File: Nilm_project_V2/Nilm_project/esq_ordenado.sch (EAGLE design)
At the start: 37 parts, among them IC1 LM1117IMPX-3.3, Q1 SMD-TRANSISTORS-NPN-25V-500MW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, Q2 SMD-TRANSISTORS-NPN-25V-500MW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, U1 ESP-32S, U2 CP2102-GM, U3 TPD2S017DBVR, U4 SP0503BAHT

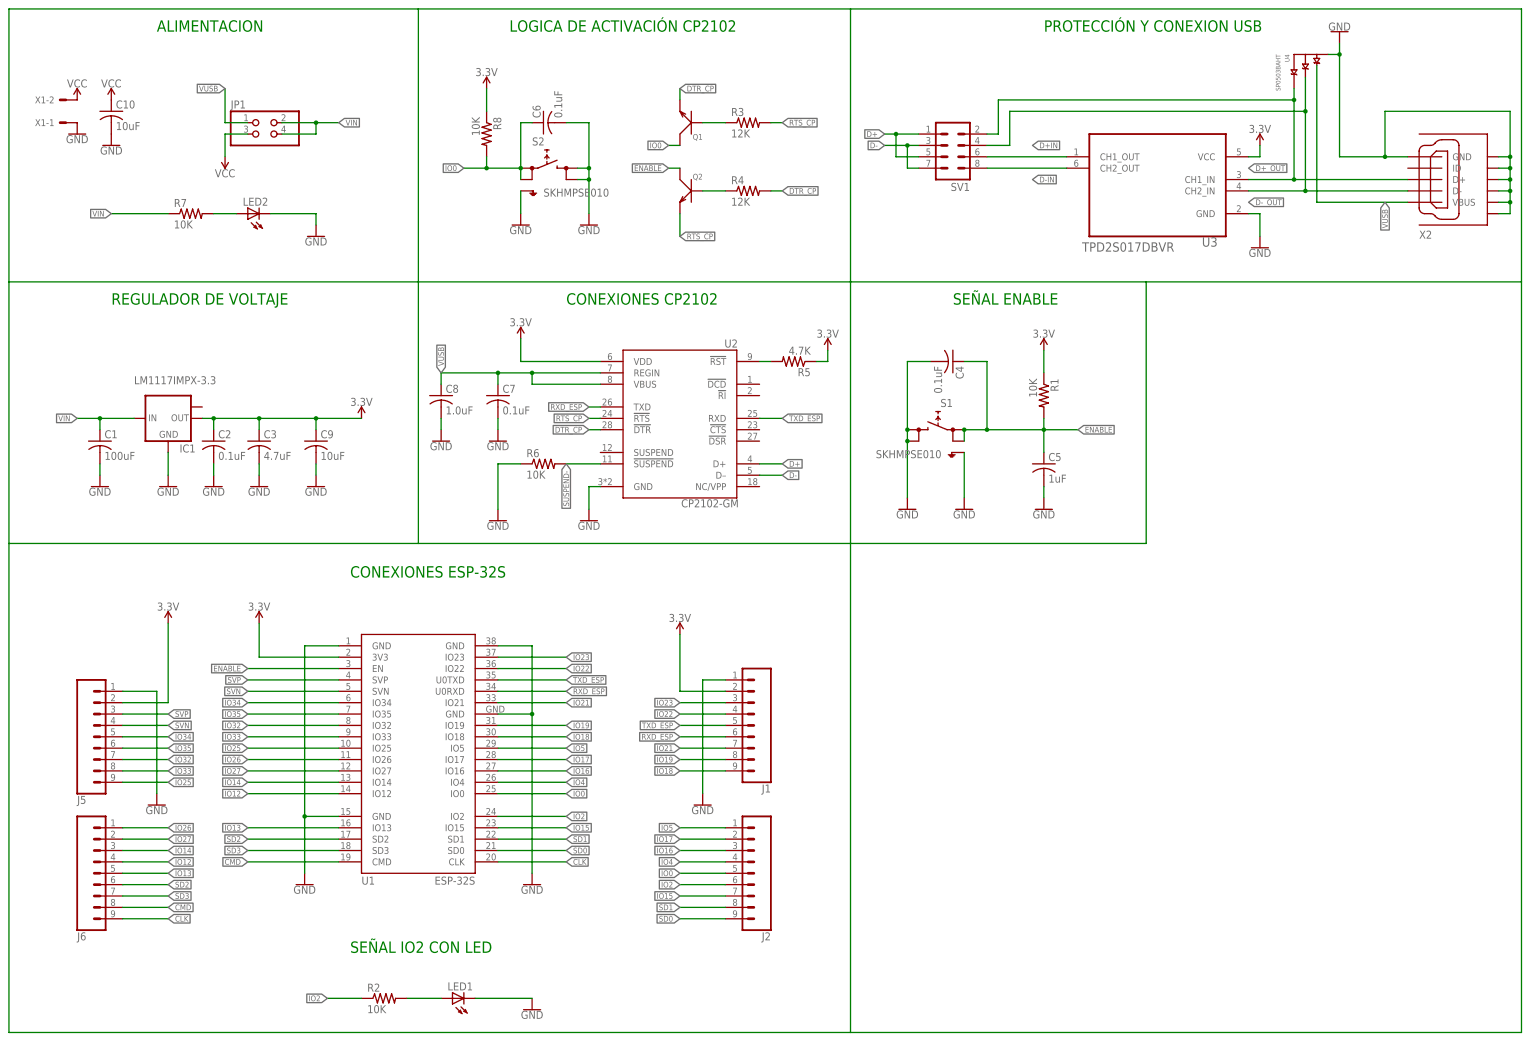
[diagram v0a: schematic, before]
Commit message: actualizacion de datahseets, lista de elementos, esquematico terminado
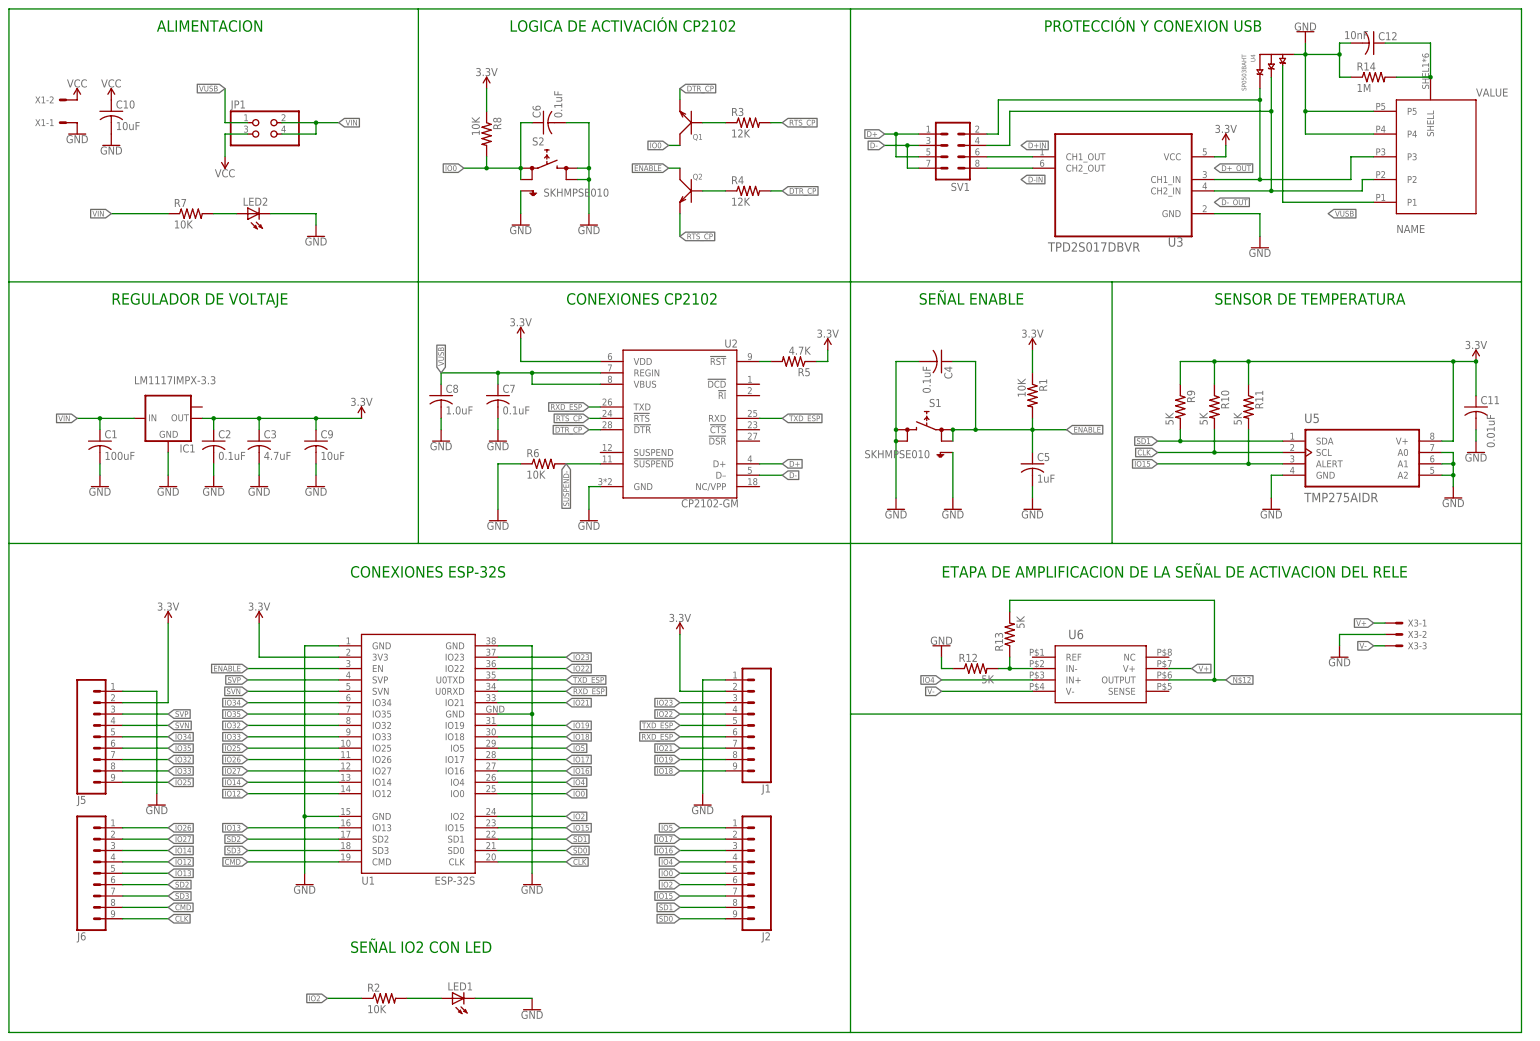
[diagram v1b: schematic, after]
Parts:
- removed X2: (no value), BeagleBone_Blue_R3:10118192-0001LF
- added C11: 0.01uF, resistor:C-USC0805
- added C12: 10nF, resistor:C-USC0805
- added R10, R11, R12, R13, R9: 5K, resistor:R-US_R0805
- added R14: 1M, resistor:R-US_R0805
- added U$1: MICRO_USB_B-AMPHENOL(10118192), usb_microB_10118192:MICRO_USB_B-AMPHENOL(10118192)
- added U5: TMP275AIDR, Sensor:TMP275AIDR
- added U6: INA157U/2K5, INA157U_2K5:INA157U/2K5D8_NIC96_SOIC8
- added X3: (no value), con-molex:KK-156-3
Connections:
- new net N$11: R12.2, R13.1, U6.IN-
- new net N$12: R13.2, U6.OUTPUT
- new net N$7: C12.1, R14.2, U$1.SHELL
- new net V+: U6.V+, X3-1.S
- new net V-: U6.V-, X3-3.S
- net 3.3V: now also C11.1, R10.1, R11.1, R9.1, U5.V+
- net CLK: now also R10.2, U5.SCL
- net D+_OUT: now also U$1.P3; no longer X2.D+
- net D-_OUT: now also U$1.P2; no longer X2.D-
- net GND: now also C11.2, C12.2, R12.1, R14.1, U$1.P4, U$1.P5, U5.A0, U5.A1, U5.A2, U5.GND, X3-2.S; no longer X2.GND, X2.SGND1, X2.SGND2, X2.SGND3, X2.SGND4, X2.SGND5, X2.SGND6
- net IO15: now also R11.2, U5.ALERT
- net IO4: now also U6.IN+
- net SD1: now also R9.2, U5.SDA
- net VUSB: now also U$1.P1; no longer X2.VBUS
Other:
- note added: "ETAPA DE AMPLIFICACION DE LA SEÑAL DE ACTIVACION DEL RELE"
- note added: "SENSOR DE TEMPERATURA"
- moved on the sheet: C4, C5, R1, S1, U3, U4

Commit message: corrección footprint switch tactile y borrado de pistas de la board
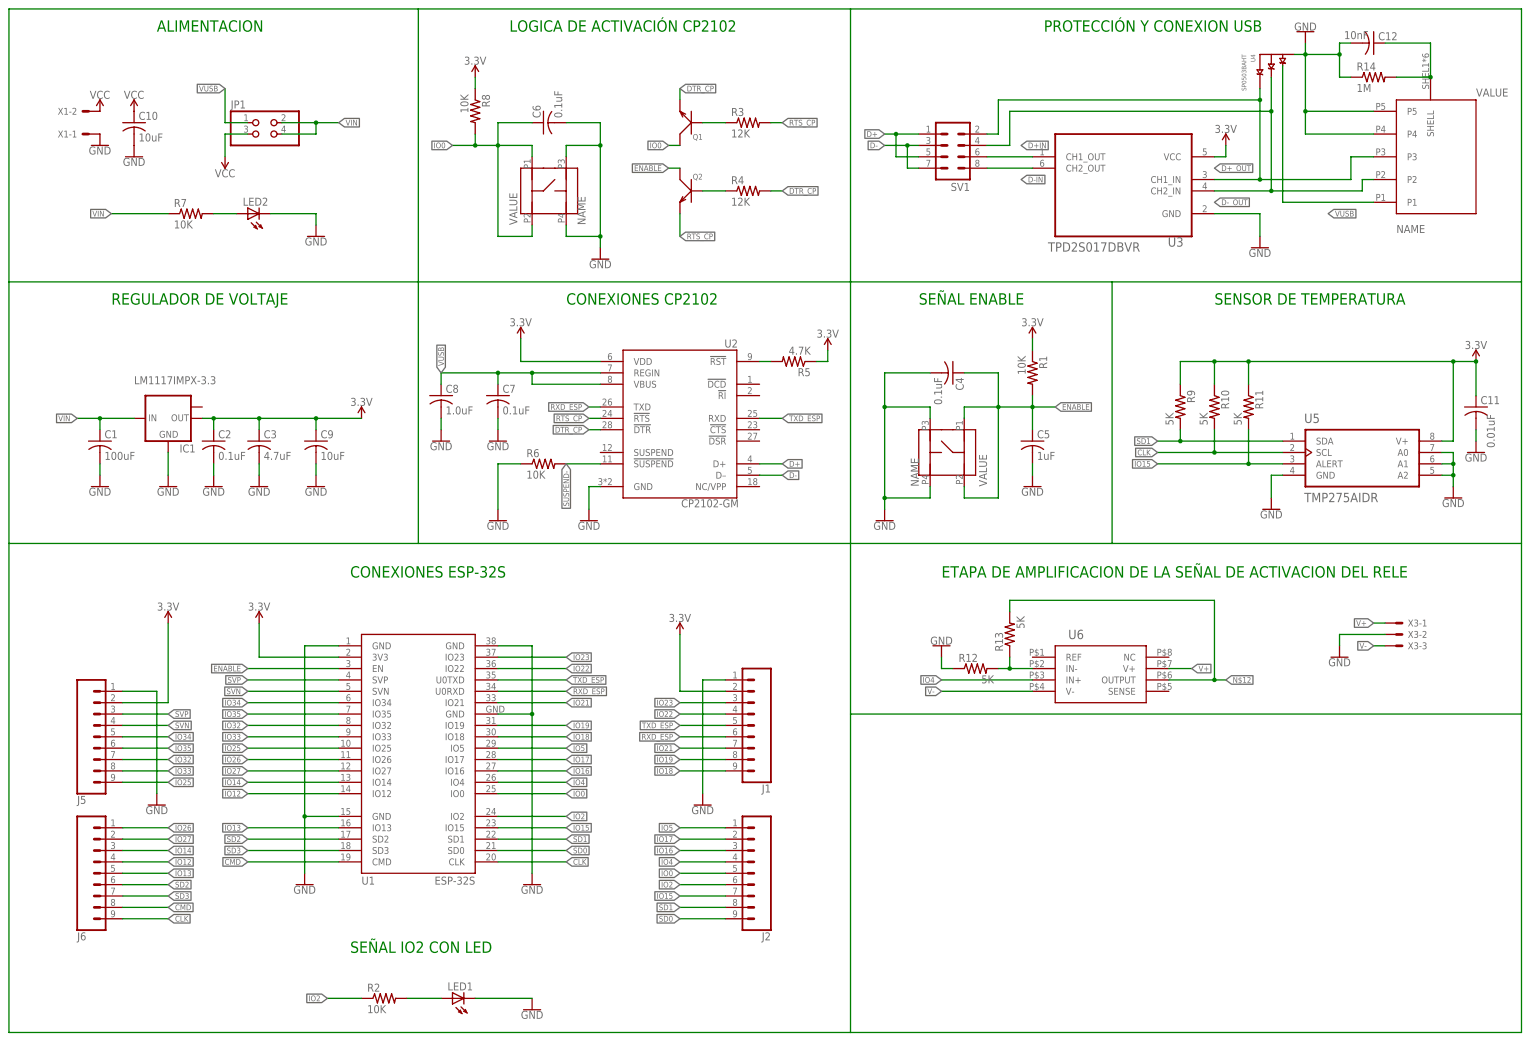
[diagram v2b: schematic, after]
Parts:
- removed S1, S2: SKHMPSE010, switch:SKHMPSE010
- added S_IO0, U$2: SWITCH_OMRON_B3FS-1012P, switch_B3FS-1012P:SWITCH_OMRON_B3FS-1012P
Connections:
- net ENABLE: now also U$2.P1, U$2.P2; no longer S1.1.1, S1.1.2
- net GND: now also S_IO0.P3, S_IO0.P4, U$2.P3, U$2.P4; no longer S1.2.1, S1.2.2, S1.SH, S2.2.1, S2.2.2, S2.SH
- net IO0: now also S_IO0.P1, S_IO0.P2; no longer S2.1.1, S2.1.2
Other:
- moved on the sheet: C10, C4, C5, R1, R8, X1-1, X1-2
